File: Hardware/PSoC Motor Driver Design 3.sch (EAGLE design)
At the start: 46 parts, among them J1 DNP, J2 DNP, J4 DNP, J5 DNP, J6 DNP, J7 DNP, J8 CORTEX_DEBUGPTH, U1 CY8C4245LQI-483, U2 DRV8835

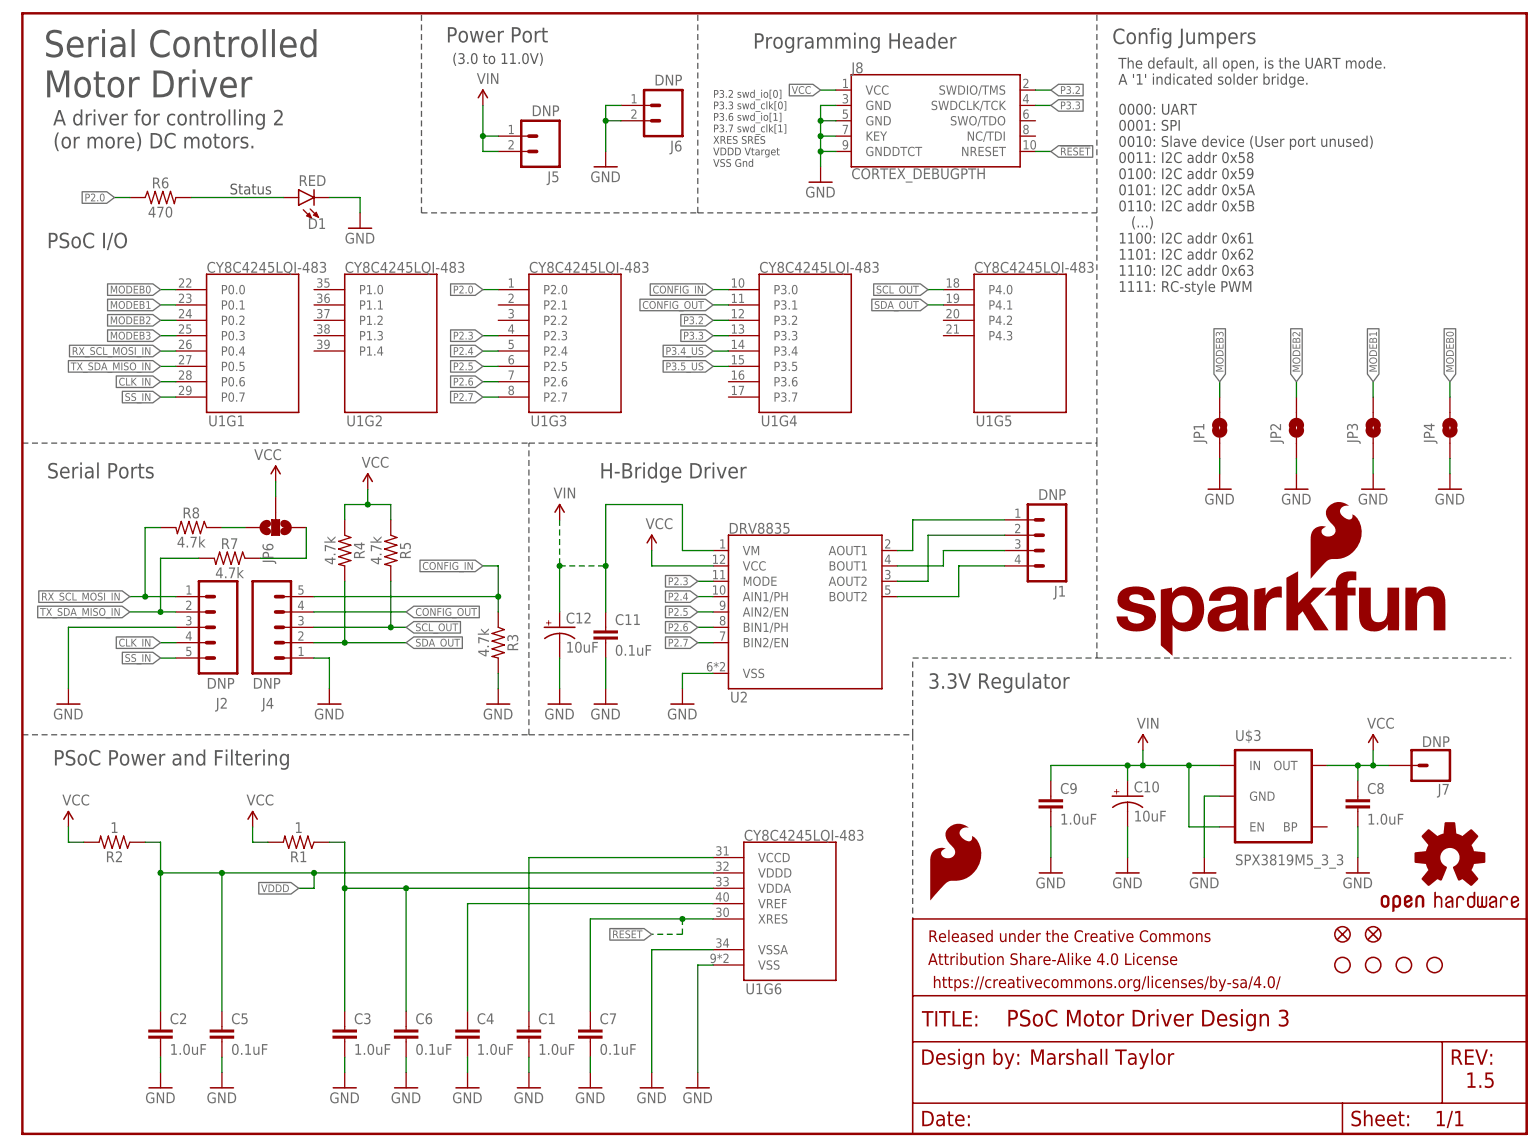
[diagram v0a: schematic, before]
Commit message: Fixed schematic naming, touched up other changes, tested 2nd serial port, reved board number
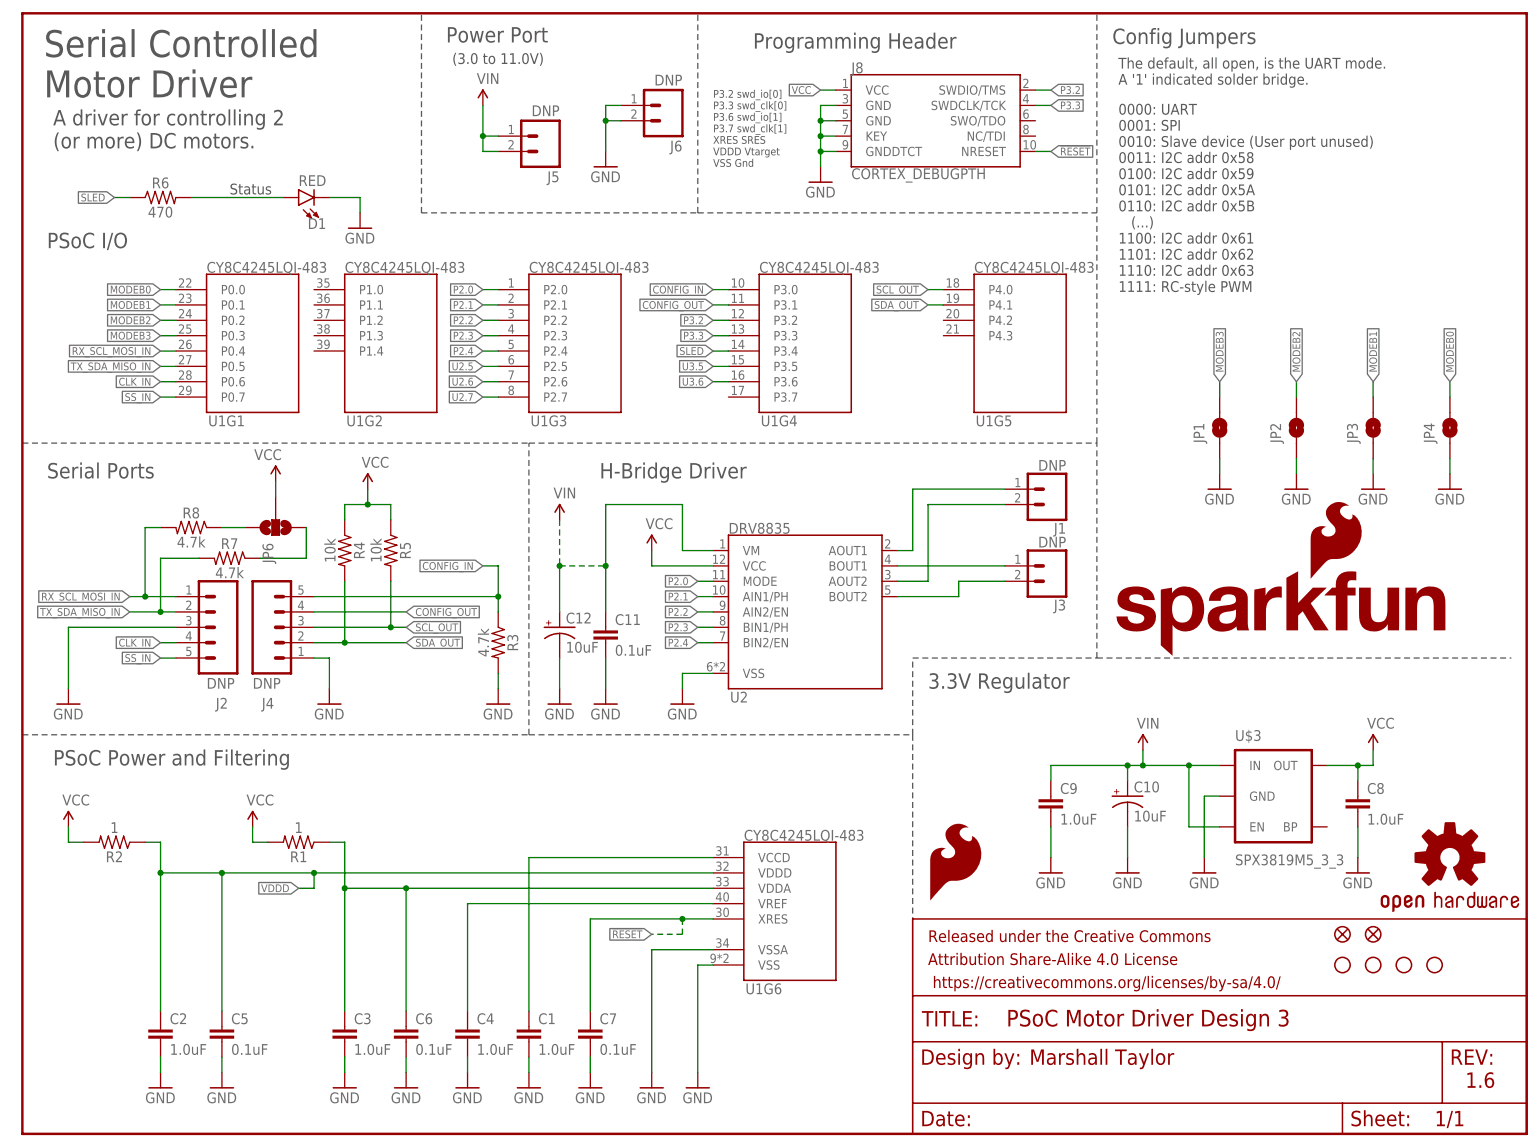
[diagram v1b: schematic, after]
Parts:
- removed J7: DNP, SparkFun-Connectors:CONN_01PTH
- added J3: DNP, SparkFun-Connectors:CONN_021X02_NO_SILK
- J1: device SparkFun-Connectors:M04PTH -> SparkFun-Connectors:CONN_021X02_NO_SILK
- R4, R5: value 4.7k -> 10k; device SparkFun-Resistors:4.7KOHM-0603-1/10W-1% -> SparkFun-Resistors:10KOHM-0603-1/10W-1%
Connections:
- net N$5 renamed AOUT1
- net N$6 renamed AOUT2
- net P3.5_US renamed U3.5
- removed net N$7: J1.3, U2.BOUT1
- removed net N$8: J1.4, U2.BOUT2
- removed net P2.5: U1G3.P2.5, U2.AIN2/EN
- removed net P2.6: U1G3.P2.6, U2.BIN1/PH
- removed net P2.7: U1G3.P2.7, U2.BIN2/EN
- removed net P3.4_US: U1G4.P3.4
- new net BOUT1: J3.1, U2.BOUT1
- new net BOUT2: J3.2, U2.BOUT2
- new net P2.1: U1G3.P2.1, U2.AIN1/PH
- new net P2.2: U1G3.P2.2, U2.AIN2/EN
- new net SLED: R6.1, U1G4.P3.4
- new net U2.5: U1G3.P2.5
- new net U2.6: U1G3.P2.6
- new net U2.7: U1G3.P2.7
- new net U3.6: U1G4.P3.6
- net P2.0: now also U2.MODE; no longer R6.1
- net P2.3: now also U2.BIN1/PH; no longer U2.MODE
- net P2.4: now also U2.BIN2/EN; no longer U2.AIN1/PH
- net VCC: no longer J7.1
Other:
- note added: "1.6"
- note removed: "1.5"
